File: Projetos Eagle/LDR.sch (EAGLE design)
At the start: 10 parts, among them J1 CONECTOR, J2 CONECTOR, U1 TL494BD

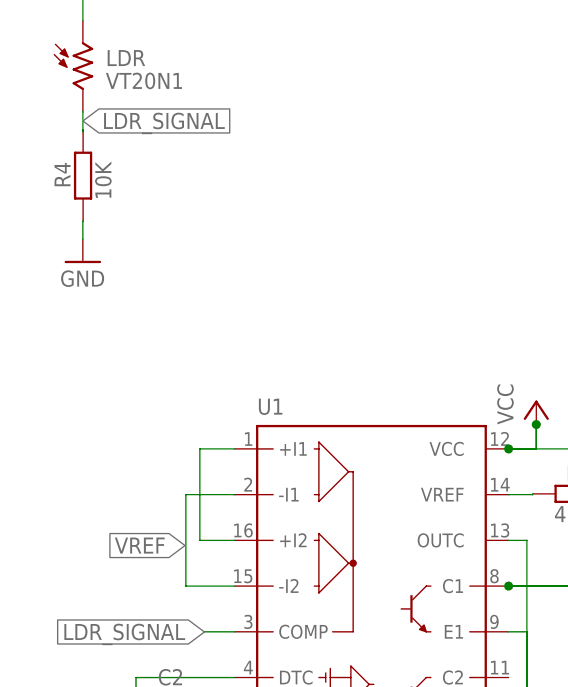
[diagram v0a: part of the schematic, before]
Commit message: correção de pads, adição de label para versionamento e plano de VCC
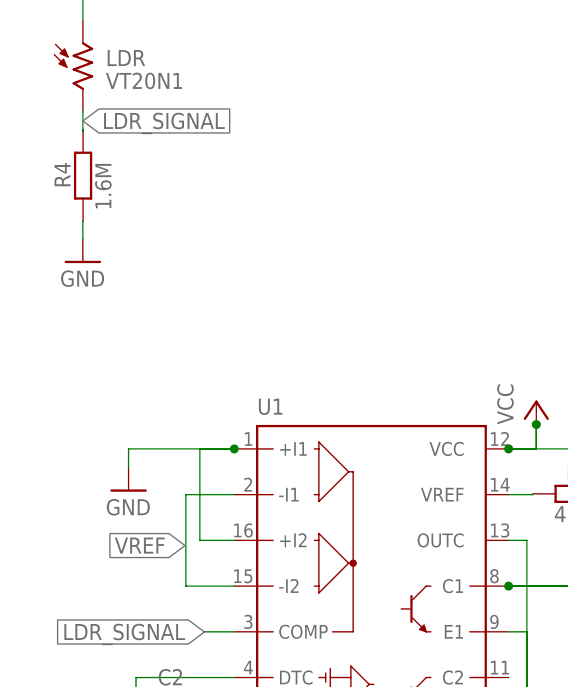
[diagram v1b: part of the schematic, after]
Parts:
- J1: value CONECTOR -> CONECTOR_MACHO; device Eletroblocks Lib:CONECTOR -> Eletroblocks Lib:CONECTOR_MACHO
- J2: value CONECTOR -> CONECTOR_FEMEA; device Eletroblocks Lib:CONECTOR -> Eletroblocks Lib:CONECTOR_FEMEA
- R4: value 10K -> 1.6M
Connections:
- removed net N$1: U1.+I1, U1.+I2
- net GND: now also U1.+I1, U1.+I2
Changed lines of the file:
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@@
 <part name="P+4" library="supply1" library_urn="urn:adsk.eagle:library:371" deviceset="VCC" device=""/>
 <part name="GND2" library="supply1" library_urn="urn:adsk.eagle:library:371" deviceset="GND" device=""/>
-<part name="J1" library="Eletroblocks Lib" deviceset="CONECTOR" device="" override_package3d_urn="urn:adsk.eagle:package:22400240/2" override_package_urn="urn:adsk.eagle:footprint:22400241/1"/>
-<part name="J2" library="Eletroblocks Lib" deviceset="CONECTOR" device="" override_package3d_urn="urn:adsk.eagle:package:22400251/2" override_package_urn="urn:adsk.eagle:footprint:22400252/1"/>
+<part name="J1" library="Eletroblocks Lib" deviceset="CONECTOR_MACHO" device="" override_package3d_urn="urn:adsk.eagle:package:22400240/2" override_package_urn="urn:adsk.eagle:footprint:22400241/1" override_locally_modified="yes"/>
+<part name="J2" library="Eletroblocks Lib" deviceset="CONECTOR_FEMEA" device="" override_package3d_urn="urn:adsk.eagle:package:22400251/2" override_package_urn="urn:adsk.eagle:footprint:22400252/1" override_locally_modified="yes"/>
 <part name="U1" library="linear" library_urn="urn:adsk.eagle:library:262" deviceset="TL494*" device="D" package3d_urn="urn:adsk.eagle:package:16423/2" technology="B"/>
 <part name="R1" library="rcl" library_urn="urn:adsk.eagle:library:334" deviceset="R-EU_" device="R0805W" package3d_urn="urn:adsk.eagle:package:23537/2" value="4K7"/>
@@
 <part name="C2" library="rcl" library_urn="urn:adsk.eagle:library:334" deviceset="C-EU" device="C0805" package3d_urn="urn:adsk.eagle:package:23617/2" value="100nF"/>
 <part name="LDR" library="photo-elements" library_urn="urn:adsk.eagle:library:323" deviceset="VT2*" device="" package3d_urn="urn:adsk.eagle:package:22223/1" override_package3d_urn="urn:adsk.eagle:package:22399586/2" override_package_urn="urn:adsk.eagle:footprint:22188/1" technology="0N1"/>
-<part name="R4" library="rcl" library_urn="urn:adsk.eagle:library:334" deviceset="R-EU_" device="R0805W" package3d_urn="urn:adsk.eagle:package:23537/2" value="10K"/>
+<part name="R4" library="rcl" library_urn="urn:adsk.eagle:library:334" deviceset="R-EU_" device="R0805W" package3d_urn="urn:adsk.eagle:package:23537/2" value="1.6M"/>
 <part name="GND4" library="supply1" library_urn="urn:adsk.eagle:library:371" deviceset="GND" device=""/>
 <part name="R3" library="eagle-ltspice" library_urn="urn:adsk.eagle:library:217" deviceset="R" device="R2512" package3d_urn="urn:adsk.eagle:package:13304/1" value="470R 1W"/>
+<part name="GND7" library="supply1" library_urn="urn:adsk.eagle:library:371" deviceset="GND" device=""/>
 </parts>
 <sheets>
@@
 <attribute name="NAME" x="78.626715625" y="162.1640125" size="1.778" layer="95" rot="R90"/>
 <attribute name="VALUE" x="83.427315625" y="162.1640125" size="1.778" layer="96" rot="R90"/>
+</instance>
+<instance part="GND7" gate="1" x="9.371440625" y="168.512" smashed="yes">
+<attribute name="VALUE" x="6.831440625" y="165.772" size="1.778" layer="96"/>
 </instance>
 </instances>
@@
 <wire x1="4.291440625" y1="198.42724375" x2="4.3169125" y2="198.42724375" width="0.1524" layer="91" grouprefs="LDR_SIGNAL1"/>
 </segment>
+<segment>
+<pinref part="U1" gate="G$1" pin="+I1"/>
+<wire x1="21.12" y1="173.14" x2="17.29095" y2="173.14" width="0.1524" layer="91" grouprefs="PWM_SIGNAL1"/>
+<wire x1="17.29095" y1="173.14" x2="17.29095" y2="162.98" width="0.1524" layer="91" grouprefs="PWM_SIGNAL1"/>
+<pinref part="U1" gate="G$1" pin="+I2"/>
+<wire x1="17.29095" y1="162.98" x2="21.12" y2="162.98" width="0.1524" layer="91" grouprefs="PWM_SIGNAL1"/>
+<pinref part="GND7" gate="1" pin="GND"/>
+<wire x1="9.371440625" y1="171.052" x2="9.371440625" y2="173.14" width="0.1524" layer="91"/>
+<wire x1="9.371440625" y1="173.14" x2="21.12" y2="173.14" width="0.1524" layer="91"/>
+<junction x="21.12" y="173.14"/>
+</segment>
 </net>
 <net name="SIGNAL_OUT" class="0">
@@
 </segment>
 </net>
-<net name="N$1" class="0">
-<segment>
-<pinref part="U1" gate="G$1" pin="+I1"/>
-<wire x1="21.12" y1="173.14" x2="17.29095" y2="173.14" width="0.1524" layer="91" grouprefs="PWM_SIGNAL1"/>
-<wire x1="17.29095" y1="173.14" x2="17.29095" y2="162.98" width="0.1524" layer="91" grouprefs="PWM_SIGNAL1"/>
-<pinref part="U1" gate="G$1" pin="+I2"/>
-<wire x1="17.29095" y1="162.98" x2="21.12" y2="162.98" width="0.1524" layer="91" grouprefs="PWM_SIGNAL1"/>
-</segment>
-</net>

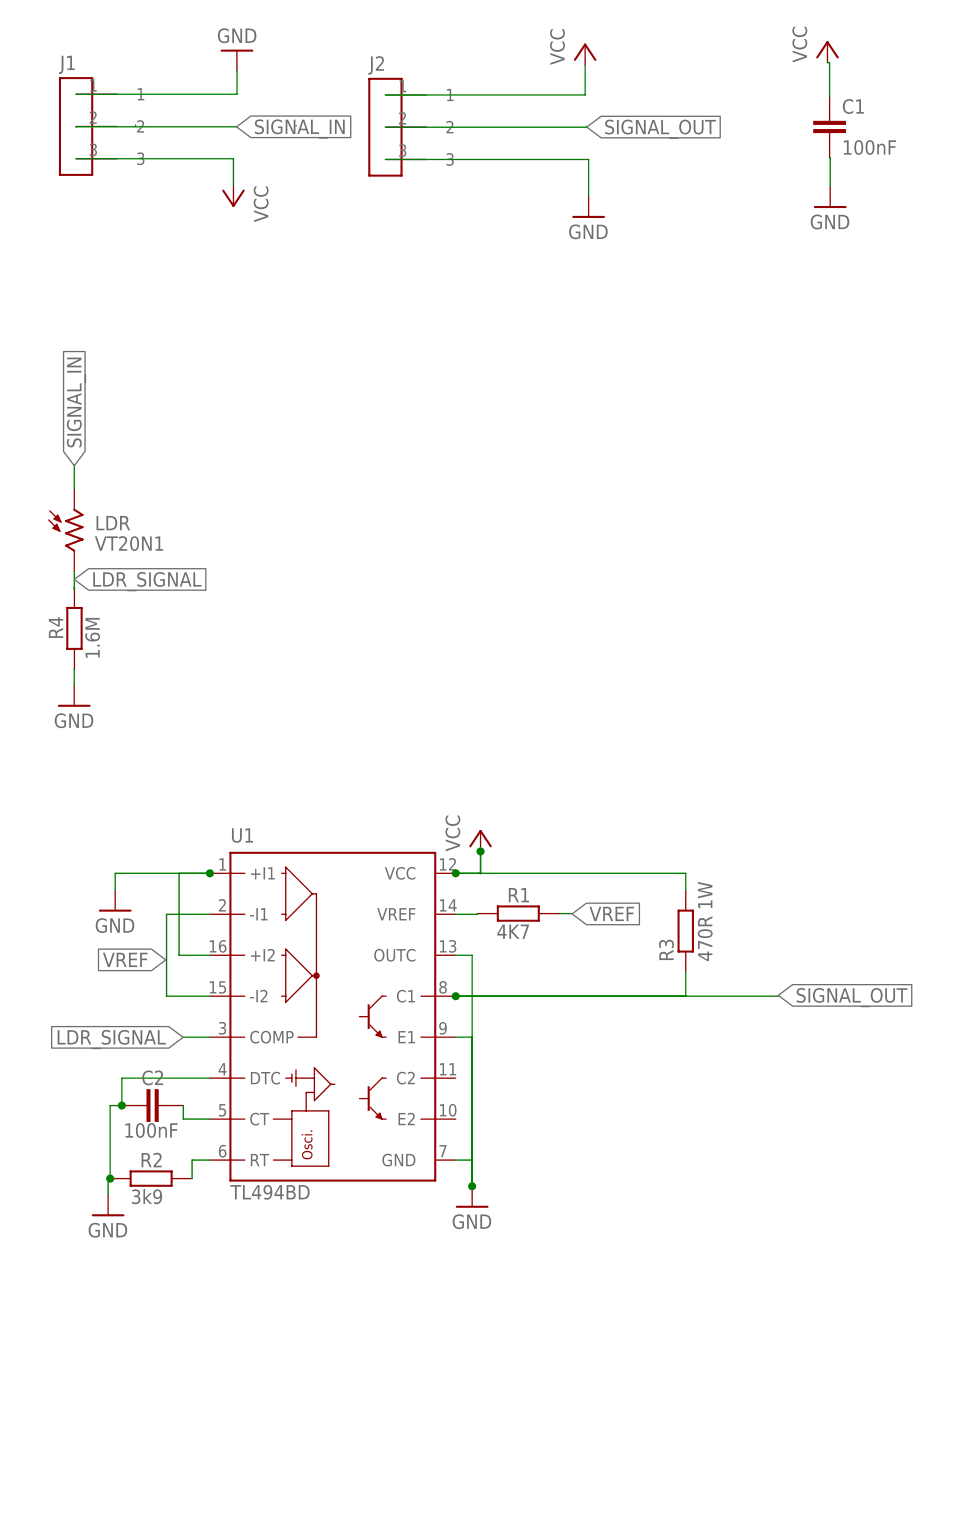
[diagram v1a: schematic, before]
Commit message: adição de filtro no SIGNAL_OUT para correção do Duty Cycle
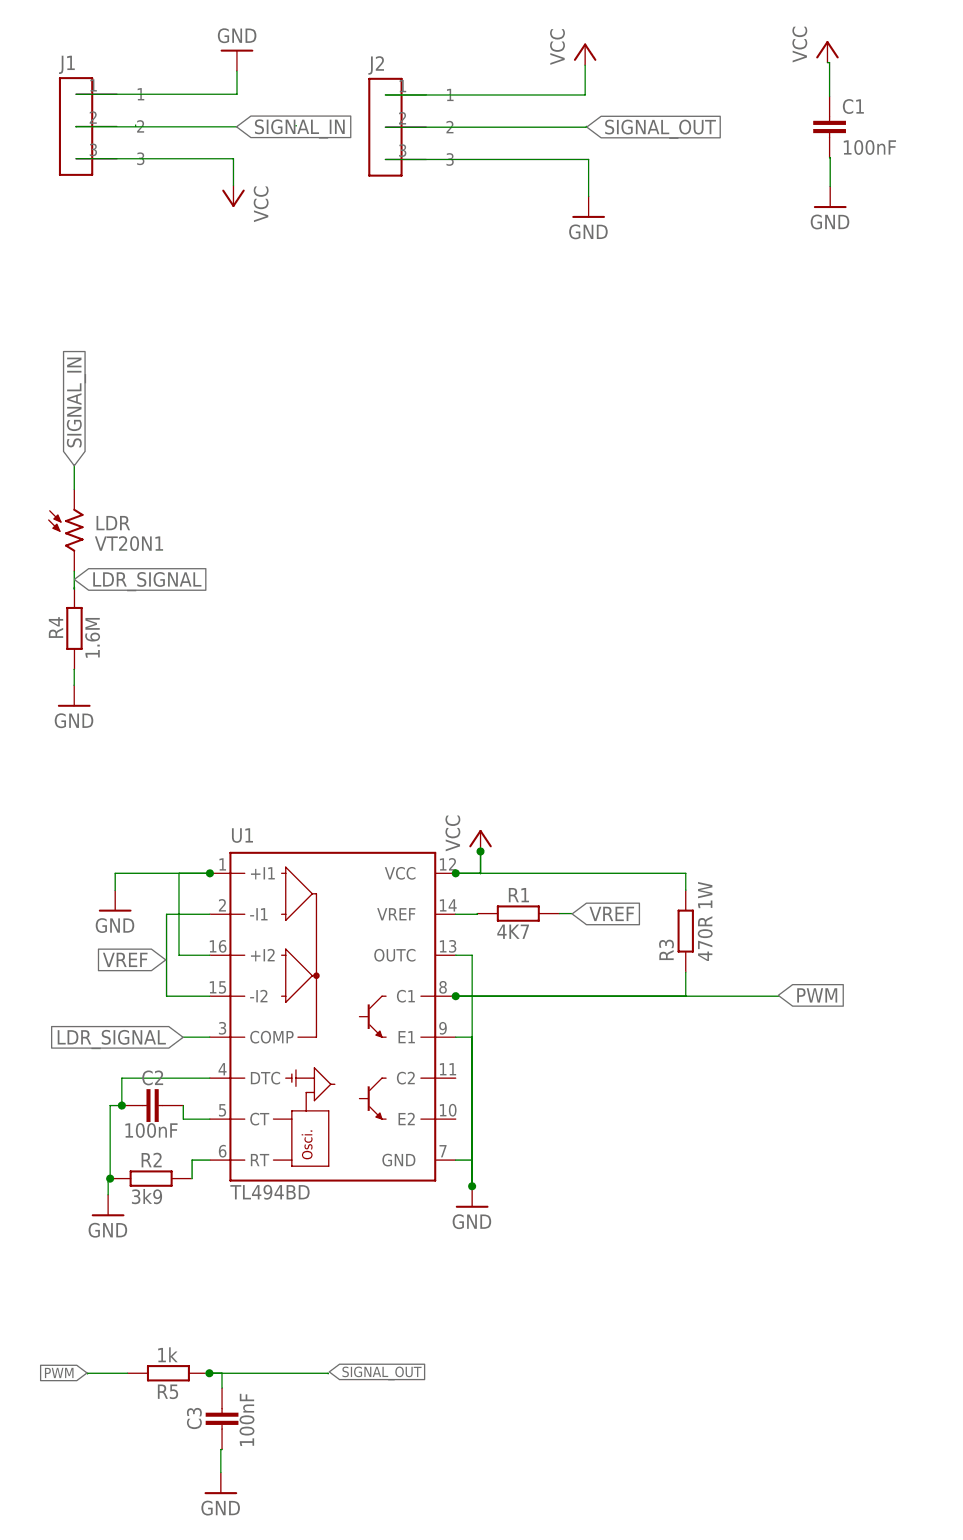
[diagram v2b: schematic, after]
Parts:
- added C3: 100nF, rcl:C-EUC0805
- added R5: 1k, rcl:R-EU_R0805W
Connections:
- new net PWM: R3.1, R5.1, U1.C1
- net GND: now also C3.1
- net SIGNAL_OUT: now also C3.2, R5.2; no longer R3.1, U1.C1
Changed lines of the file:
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@@
 <schematic_group name="PWM_SIGNAL1"/>
 <schematic_group name="LDR_SIGNAL1"/>
+<schematic_group name="FILTER"/>
 </groups>
 <parts>
@@
 <part name="R3" library="eagle-ltspice" library_urn="urn:adsk.eagle:library:217" deviceset="R" device="R2512" package3d_urn="urn:adsk.eagle:package:13304/1" value="470R 1W"/>
 <part name="GND7" library="supply1" library_urn="urn:adsk.eagle:library:371" deviceset="GND" device=""/>
+<part name="R5" library="rcl" library_urn="urn:adsk.eagle:library:334" deviceset="R-EU_" device="R0805W" package3d_urn="urn:adsk.eagle:package:23537/2" value="1k"/>
+<part name="C3" library="rcl" library_urn="urn:adsk.eagle:library:334" deviceset="C-EU" device="C0805" package3d_urn="urn:adsk.eagle:package:23617/2" value="100nF"/>
+<part name="GND8" library="supply1" library_urn="urn:adsk.eagle:library:371" deviceset="GND" device=""/>
 </parts>
 <sheets>
@@
 <instance part="GND7" gate="1" x="9.371440625" y="168.512" smashed="yes">
 <attribute name="VALUE" x="6.831440625" y="165.772" size="1.778" layer="96"/>
+</instance>
+<instance part="R5" gate="G$1" x="15.974575" y="111.142634375" smashed="yes" grouprefs="FILTER">
+<attribute name="NAME" x="17.368559375" y="109.746728125" size="1.778" layer="95" rot="R180"/>
+<attribute name="VALUE" x="14.4607375" y="112.5066125" size="1.778" layer="96"/>
+</instance>
+<instance part="C3" gate="G$1" x="22.62181875" y="104.225721875" smashed="yes" rot="R180" grouprefs="FILTER">
+<attribute name="NAME" x="18.30281875" y="107.021721875" size="1.778" layer="95" rot="R270"/>
+<attribute name="VALUE" x="24.82281875" y="108.721721875" size="1.778" layer="96" rot="R270"/>
+</instance>
+<instance part="GND8" gate="1" x="22.47671875" y="96.276721875" smashed="yes" grouprefs="FILTER">
+<attribute name="VALUE" x="19.93671875" y="93.536721875" size="1.778" layer="96"/>
 </instance>
 </instances>
@@
 <junction x="21.12" y="173.14"/>
 </segment>
+<segment>
+<pinref part="GND8" gate="1" pin="GND"/>
+<pinref part="C3" gate="G$1" pin="1"/>
+<wire x1="22.47671875" y1="98.816721875" x2="22.47671875" y2="101.685721875" width="0.1524" layer="91" grouprefs="FILTER"/>
+<wire x1="22.47671875" y1="101.685721875" x2="22.62181875" y2="101.685721875" width="0.1524" layer="91" grouprefs="FILTER"/>
+</segment>
 </net>
 <net name="SIGNAL_OUT" class="0">
@@
 </segment>
 <segment>
-<pinref part="U1" gate="G$1" pin="C1"/>
-<wire x1="51.6" y1="157.9" x2="91.7" y2="157.9" width="0.1524" layer="91" grouprefs="PWM_SIGNAL1"/>
-<label x="91.6" y="158" size="1.778" layer="95" xref="yes" grouprefs="PWM_SIGNAL1"/>
-<pinref part="R3" gate="G$1" pin="1"/>
-<wire x1="80.125315625" y1="160.8940125" x2="80.125315625" y2="157.9" width="0.1524" layer="91"/>
-<wire x1="80.125315625" y1="157.9" x2="51.6" y2="157.9" width="0.1524" layer="91"/>
-<junction x="51.6" y="157.9"/>
+<pinref part="R5" gate="G$1" pin="2"/>
+<pinref part="C3" gate="G$1" pin="2"/>
+<wire x1="21.054575" y1="111.142634375" x2="22.62181875" y2="111.142634375" width="0.1524" layer="91" grouprefs="FILTER"/>
+<wire x1="22.62181875" y1="111.142634375" x2="22.62181875" y2="109.305721875" width="0.1524" layer="91" grouprefs="FILTER"/>
+<wire x1="21.054575" y1="111.142634375" x2="35.78351875" y2="111.142634375" width="0.1524" layer="91" grouprefs="FILTER"/>
+<wire x1="35.78351875" y1="111.142634375" x2="35.78351875" y2="111.0716625" width="0.1524" layer="91" grouprefs="FILTER"/>
+<junction x="21.054575" y="111.142634375" grouprefs="FILTER"/>
+<label x="35.920678125" y="111.310421875" size="1.27" layer="95" xref="yes" grouprefs="FILTER"/>
 </segment>
 </net>
@@
 </segment>
 </net>
+<net name="PWM" class="0">
+<segment>
+<pinref part="R5" gate="G$1" pin="1"/>
+<wire x1="10.894575" y1="111.142634375" x2="5.948678125" y2="111.142634375" width="0.1524" layer="91" grouprefs="FILTER"/>
+<wire x1="5.948678125" y1="111.142634375" x2="5.948678125" y2="111.048803125" width="0.1524" layer="91" grouprefs="FILTER"/>
+<label x="5.877559375" y="111.178340625" size="1.27" layer="95" rot="R180" xref="yes" grouprefs="FILTER"/>
+</segment>
+<segment>
+<pinref part="U1" gate="G$1" pin="C1"/>
+<wire x1="51.6" y1="157.9" x2="91.7" y2="157.9" width="0.1524" layer="91" grouprefs="PWM_SIGNAL1"/>
+<label x="91.6" y="158" size="1.778" layer="95" xref="yes" grouprefs="PWM_SIGNAL1"/>
+<pinref part="R3" gate="G$1" pin="1"/>
+<wire x1="80.125315625" y1="160.8940125" x2="80.125315625" y2="157.9" width="0.1524" layer="91"/>
+<wire x1="80.125315625" y1="157.9" x2="51.6" y2="157.9" width="0.1524" layer="91"/>
+<junction x="51.6" y="157.9"/>
+</segment>
+</net>
